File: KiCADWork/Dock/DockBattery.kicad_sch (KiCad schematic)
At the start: 0 parts

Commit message: Dock Updates
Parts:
- added BT2: Battery, easyeda2kicad:CONN-TH_S2B-PH-K-LF-SN, symbol Device:Battery
- added C1, C3: 10u, Capacitor_SMD:C_0402_1005Metric_Pad0.74x0.62mm_HandSolder, symbol Device:C
- added C2 (x2): 1u, Capacitor_SMD:C_0402_1005Metric_Pad0.74x0.62mm_HandSolder, symbol Device:C
- added C2: 100n, Capacitor_SMD:C_0402_1005Metric_Pad0.74x0.62mm_HandSolder, symbol Device:C
- added D1: WHITE LED, LED_SMD:LED_0603_1608Metric_Pad1.05x0.95mm_HandSolder, symbol Device:LED
- added R1, R3: 2k, Resistor_SMD:R_0402_1005Metric_Pad0.72x0.64mm_HandSolder, symbol Device:R
- added R2: 100, Resistor_SMD:R_0402_1005Metric_Pad0.72x0.64mm_HandSolder, symbol Device:R
- added U1: MCP73831T-2ACI/OT, easyeda2kicad:SOT-23-5_L3.0-W1.7-P0.95-LS2.8-BL, symbol easyeda2kicad:MCP73831T-2ACI_OT
- added U2: XB6096I2SV, easyeda2kicad:WDFN-6_L2.0-W2.0-P0.65-BL-EP, symbol easyeda2kicad:XB6096I2SV
- added U4: PJ9193M33SE, easyeda2kicad:SSOP-5_L2.9-W1.6-P0.95-LS2.8-BR, symbol easyeda2kicad:PJ9193M33SE
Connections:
- new net: R3.1, U1.5 (PROG)
- new net: D1.1 (K), R1.1
- new net: R1.2, U1.1 (STAT)
- new net: BT2.1 (+), R2.1
- new net: BT2.2 (-), U2.2 (GND), U2.3 (GND), U2.7 (EP)
- new net +3V3: C2.1, U4.5 (VOUT)
- new net GND: C1.2, C2.2, C2.2, C2.2, C3.2, R3.2, U1.2 (VSS), U2.4 (VM), U2.5 (VM), U2.6 (VM), U4.2 (GND)
- new net VBAT: C1.1, C2.1, C2.1, R2.2, U1.3 (VBAT), U2.1 (VDD), U4.1 (VIN), U4.3 (EN)
- new net VBUS: C3.1, D1.2 (A), U1.4 (VDD)
- no-connect marks 0 -> 1

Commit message: Ignoring Backups
More Dock progress
All local backups removed
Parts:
- removed C1, C3: 10u, Capacitor_SMD:C_0402_1005Metric_Pad0.74x0.62mm_HandSolder, symbol Device:C
- removed C2: 100n, Capacitor_SMD:C_0402_1005Metric_Pad0.74x0.62mm_HandSolder, symbol Device:C
- removed D1: WHITE LED, LED_SMD:LED_0603_1608Metric_Pad1.05x0.95mm_HandSolder, symbol Device:LED
- removed R1, R3: 2k, Resistor_SMD:R_0402_1005Metric_Pad0.72x0.64mm_HandSolder, symbol Device:R
- removed R2: 100, Resistor_SMD:R_0402_1005Metric_Pad0.72x0.64mm_HandSolder, symbol Device:R
- removed U1: MCP73831T-2ACI/OT, easyeda2kicad:SOT-23-5_L3.0-W1.7-P0.95-LS2.8-BL, symbol easyeda2kicad:MCP73831T-2ACI_OT
- removed U2: XB6096I2SV, easyeda2kicad:WDFN-6_L2.0-W2.0-P0.65-BL-EP, symbol easyeda2kicad:XB6096I2SV
- removed U4: PJ9193M33SE, easyeda2kicad:SSOP-5_L2.9-W1.6-P0.95-LS2.8-BR, symbol easyeda2kicad:PJ9193M33SE
- added C12, C6: 4.7u, Capacitor_SMD:C_0402_1005Metric_Pad0.74x0.62mm_HandSolder, symbol Device:C
- added C15: 10u, Capacitor_SMD:C_0402_1005Metric_Pad0.74x0.62mm_HandSolder, symbol Device:C
- added C16, C17: 22u, Capacitor_SMD:C_0603_1608Metric_Pad1.08x0.95mm_HandSolder, symbol Device:C
- added C5: 1u, Capacitor_SMD:C_0402_1005Metric_Pad0.74x0.62mm_HandSolder, symbol Device:C
- added D1: BLUE RED, LED_SMD:LED_0603_1608Metric_Pad1.05x0.95mm_HandSolder, symbol Device:LED
- added D1: BLUE LED, LED_SMD:LED_0603_1608Metric_Pad1.05x0.95mm_HandSolder, symbol Device:LED
- added L1: 4.7u, easyeda2kicad:IND-SMD_L5.2-W5.2_YSPI0530, symbol Device:L
- added R12: 100k, Resistor_SMD:R_0402_1005Metric_Pad0.72x0.64mm_HandSolder, symbol Device:R
- added R12: 1.78k, Resistor_SMD:R_0402_1005Metric_Pad0.72x0.64mm_HandSolder, symbol Device:R
- added R12 (x3): 1.18k, Resistor_SMD:R_0402_1005Metric_Pad0.72x0.64mm_HandSolder, symbol Device:R
- added R12: 10k, Resistor_SMD:R_0402_1005Metric_Pad0.72x0.64mm_HandSolder, symbol Device:R
- added R12: 732, Resistor_SMD:R_0402_1005Metric_Pad0.72x0.64mm_HandSolder, symbol Device:R
- added U2: TPS61023DRLR, easyeda2kicad:SOT-563_L1.6-W1.2-P0.50-LS1.6-BR, symbol easyeda2kicad:TPS61023DRLR
- added U3: AMS1117-3.3, Package_TO_SOT_SMD:SOT-223-3_TabPin2, symbol Regulator_Linear:AMS1117-3.3
- added U4: BQ24073RGT, Package_DFN_QFN:VQFN-16-1EP_3x3mm_P0.5mm_EP1.6x1.6mm, symbol Battery_Management:BQ24073RGT
- BT2: LCSC Part (none) -> C173752
- C13, C14: renamed from C2; value 1u -> 2.2u; LCSC Part (none) -> C12530
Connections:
- net +3V3: now also U3.2 (VO)
- net GND: now also BT2.2 (-), C12.2, C15.2, C16.2, C17.2, C5.2, C6.2, R12.1, R12.1, R12.2, R12.2, U2.4 (GND), U3.1 (GND), U4.14 (TMR), U4.17 (VSS), U4.4 (~{CE}), U4.6 (EN1), U4.8 (VSS)
- net VBUS: now also C5.1, U4.13 (IN)
- net at BT2.1 (+): now also C12.1, U4.2 (BAT), U4.3 (BAT)
- net VBAT renamed Vsys
- net Vsys: now also C16.1, C17.1, R12.2, R12.2, U2.6 (VOUT), U3.3 (VI)
- new net: L1.1, U2.3 (VIN)
- new net: C15.1, C6.1, L1.2, R12.2, R12.2, U2.2 (EN), U2.5 (SW), U4.10 (OUT), U4.11 (OUT), U4.5 (EN2)
- new net: R12.1, U4.16 (ISET)
- new net: D1.2 (A), R12.1 (x2)
- new net: D1.1 (K), U4.7 (~{PGOOD})
- new net: R12.1, U2.1 (FB)
- new net: D1.1 (K), U4.9 (~{CHG})
- new net: R12.2, U4.1 (TS)
- new net: R12.1, U4.12 (ILIM)
- no-connect marks 1 -> 0
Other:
- moved on the sheet: BT2, C13, C14

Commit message: Beautiful Skilkscreen Added
Dock schematic intial draft complete
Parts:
- added D5: LED, LED_SMD:LED_0603_1608Metric_Pad1.05x0.95mm_HandSolder, symbol Device:LED
- added R12: 2k, Resistor_SMD:R_0402_1005Metric_Pad0.72x0.64mm_HandSolder, symbol Device:R
- added TP1 (x5): TestPoint, TestPoint:TestPoint_Pad_D1.0mm, symbol Connector:TestPoint
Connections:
- net +3V3: now also R12.2, TP1.1
- net GND: now also D5.1 (K)
- net VBUS: now also TP1.1
- net Vsys: now also TP1.1
- net at C15.1, C6.1, L1.2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: now also TP1.1
- net at BT2.1 (+), C12.1, U4.2 (BAT)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: now also TP1.1
- new net: D5.2 (A), R12.1

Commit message: Small Updates
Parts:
- D1: footprint LED_SMD:LED_0603_1608Metric_Pad1.05x0.95mm_HandSolder -> easyeda2kicad:SideStuckLED
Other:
- moved on the sheet: D5, R12
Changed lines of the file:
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@@
     (stroke (width 0) (type default))
   )
-  (wire (pts (xy 117.475 153.035) (xy 117.475 160.655))
+  (wire (pts (xy 108.585 163.83) (xy 108.585 171.45))
     (stroke (width 0) (type default))
   )
@@
     (stroke (width 0) (type default))
   )
-  (wire (pts (xy 117.475 139.7) (xy 117.475 145.415))
+  (wire (pts (xy 108.585 150.495) (xy 108.585 156.21))
     (stroke (width 0) (type default))
   )
@@
     (stroke (width 0) (type default))
   )
-  (wire (pts (xy 117.475 130.81) (xy 117.475 132.08))
+  (wire (pts (xy 108.585 141.605) (xy 108.585 142.875))
     (stroke (width 0) (type default))
   )
@@
     (effects (font (size 3 3)) (justify left bottom))
   )
-  (label "Power Indicator" (at 120.015 146.05 0) (fields_autoplaced)
+  (label "Power Indicator" (at 111.125 156.845 0) (fields_autoplaced)
     (effects (font (size 2 2)) (justify left bottom))
   )
@@
     (effects (font (size 1.27 1.27)) (justify right))
   )
-  (symbol (lib_id "Device:LED") (at 117.475 149.225 90) (unit 1)
-    (in_bom yes) (on_board yes) (dnp no) (fields_autoplaced)
-    (property "Reference" "D5" (at 120.65 149.5425 90)
+  (symbol (lib_id "Device:LED") (at 108.585 160.02 90) (unit 1)
+    (in_bom yes) (on_board yes) (dnp no) (fields_autoplaced)
+    (property "Reference" "D5" (at 111.76 160.3375 90)
       (effects (font (size 1.27 1.27)) (justify right))
     )
-    (property "Value" "LED" (at 120.65 152.0825 90)
+    (property "Value" "LED" (at 111.76 162.8775 90)
       (effects (font (size 1.27 1.27)) (justify right))
     )
-    (property "Footprint" "LED_SMD:LED_0603_1608Metric_Pad1.05x0.95mm_HandSolder" (at 117.475 149.225 0)
-      (effects (font (size 1.27 1.27)) hide)
-    )
-    (property "Datasheet" "~" (at 117.475 149.225 0)
+    (property "Footprint" "LED_SMD:LED_0603_1608Metric_Pad1.05x0.95mm_HandSolder" (at 108.585 160.02 0)
+      (effects (font (size 1.27 1.27)) hide)
+    )
+    (property "Datasheet" "~" (at 108.585 160.02 0)
       (effects (font (size 1.27 1.27)) hide)
     )
@@
     )
   )
-  (symbol (lib_id "power:GND") (at 117.475 160.655 0) (unit 1)
-    (in_bom yes) (on_board yes) (dnp no) (fields_autoplaced)
-    (property "Reference" "#PWR023" (at 117.475 167.005 0)
-      (effects (font (size 1.27 1.27)) hide)
-    )
-    (property "Value" "GND" (at 117.475 165.735 0)
-      (effects (font (size 1.27 1.27)))
-    )
-    (property "Footprint" "" (at 117.475 160.655 0)
-      (effects (font (size 1.27 1.27)) hide)
-    )
-    (property "Datasheet" "" (at 117.475 160.655 0)
+  (symbol (lib_id "power:GND") (at 108.585 171.45 0) (unit 1)
+    (in_bom yes) (on_board yes) (dnp no) (fields_autoplaced)
+    (property "Reference" "#PWR023" (at 108.585 177.8 0)
+      (effects (font (size 1.27 1.27)) hide)
+    )
+    (property "Value" "GND" (at 108.585 176.53 0)
+      (effects (font (size 1.27 1.27)))
+    )
+    (property "Footprint" "" (at 108.585 171.45 0)
+      (effects (font (size 1.27 1.27)) hide)
+    )
+    (property "Datasheet" "" (at 108.585 171.45 0)
       (effects (font (size 1.27 1.27)) hide)
     )
@@
       (effects (font (size 1.27 1.27)) (justify left))
     )
-    (property "Footprint" "LED_SMD:LED_0603_1608Metric_Pad1.05x0.95mm_HandSolder" (at 127 77.47 0)
+    (property "Footprint" "easyeda2kicad:SideStuckLED" (at 127 77.47 0)
       (effects (font (size 1.27 1.27)) hide)
     )
@@
       (effects (font (size 1.27 1.27)) (justify left))
     )
-    (property "Footprint" "LED_SMD:LED_0603_1608Metric_Pad1.05x0.95mm_HandSolder" (at 137.16 78.105 0)
+    (property "Footprint" "easyeda2kicad:SideStuckLED" (at 137.16 78.105 0)
       (effects (font (size 1.27 1.27)) hide)
     )
@@
     )
   )
-  (symbol (lib_id "Device:R") (at 117.475 135.89 180) (unit 1)
-    (in_bom yes) (on_board yes) (dnp no)
-    (property "Reference" "R12" (at 112.395 135.89 90)
-      (effects (font (size 1.27 1.27)))
-    )
-    (property "Value" "2k" (at 114.935 135.89 90)
-      (effects (font (size 1.27 1.27)))
-    )
-    (property "Footprint" "Resistor_SMD:R_0402_1005Metric_Pad0.72x0.64mm_HandSolder" (at 119.253 135.89 90)
-      (effects (font (size 1.27 1.27)) hide)
-    )
-    (property "Datasheet" "~" (at 117.475 135.89 0)
-      (effects (font (size 1.27 1.27)) hide)
-    )
-    (property "LCSC Part" "C3016052" (at 117.475 135.89 0)
+  (symbol (lib_id "Device:R") (at 108.585 146.685 180) (unit 1)
+    (in_bom yes) (on_board yes) (dnp no)
+    (property "Reference" "R12" (at 103.505 146.685 90)
+      (effects (font (size 1.27 1.27)))
+    )
+    (property "Value" "2k" (at 106.045 146.685 90)
+      (effects (font (size 1.27 1.27)))
+    )
+    (property "Footprint" "Resistor_SMD:R_0402_1005Metric_Pad0.72x0.64mm_HandSolder" (at 110.363 146.685 90)
+      (effects (font (size 1.27 1.27)) hide)
+    )
+    (property "Datasheet" "~" (at 108.585 146.685 0)
+      (effects (font (size 1.27 1.27)) hide)
+    )
+    (property "LCSC Part" "C3016052" (at 108.585 146.685 0)
       (effects (font (size 1.27 1.27)) hide)
     )
@@
     )
   )
-  (symbol (lib_id "power:+3V3") (at 117.475 130.81 0) (unit 1)
-    (in_bom yes) (on_board yes) (dnp no) (fields_autoplaced)
-    (property "Reference" "#PWR022" (at 117.475 134.62 0)
-      (effects (font (size 1.27 1.27)) hide)
-    )
-    (property "Value" "+3V3" (at 117.475 125.73 0)
-      (effects (font (size 1.27 1.27)))
-    )
-    (property "Footprint" "" (at 117.475 130.81 0)
-      (effects (font (size 1.27 1.27)) hide)
-    )
-    (property "Datasheet" "" (at 117.475 130.81 0)
-      (effects (font (size 1.27 1.27)) hide)
-    )
+  (symbol (lib_id "power:+3V3") (at 108.585 141.605 0) (unit 1)
+    (in_bom yes) (on_board yes) (dnp no) (fields_autoplaced)
+    (property "Reference" "#PWR022" (at 108.585 145.415 0)
+      (effects (font (size 1.27 1.27)) hide)
+    )
+    (property "Value" "+3V3" (at 108.585 136.525 0)
+      (effects (font (size 1.27 1.27)))
+    )
+    (property "Footprint" "" (at 108.585 141.605 0)
+      (effects (font (size 1.27 1.27)) hide)
+    )
+    (property "Datasheet" "" (at 108.585 141.605 0)
+      (effects (font (size 1.27 1.27)) hide)
+    )

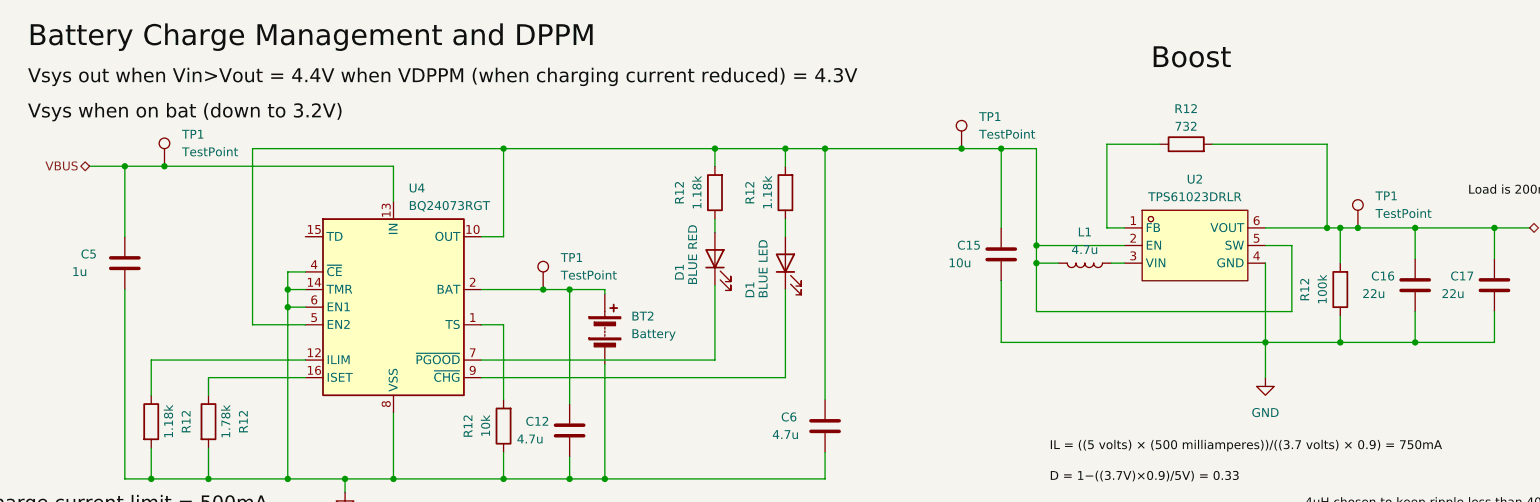
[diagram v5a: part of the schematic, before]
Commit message: Dock Updates
Starting to layout the dock
Dom still to check
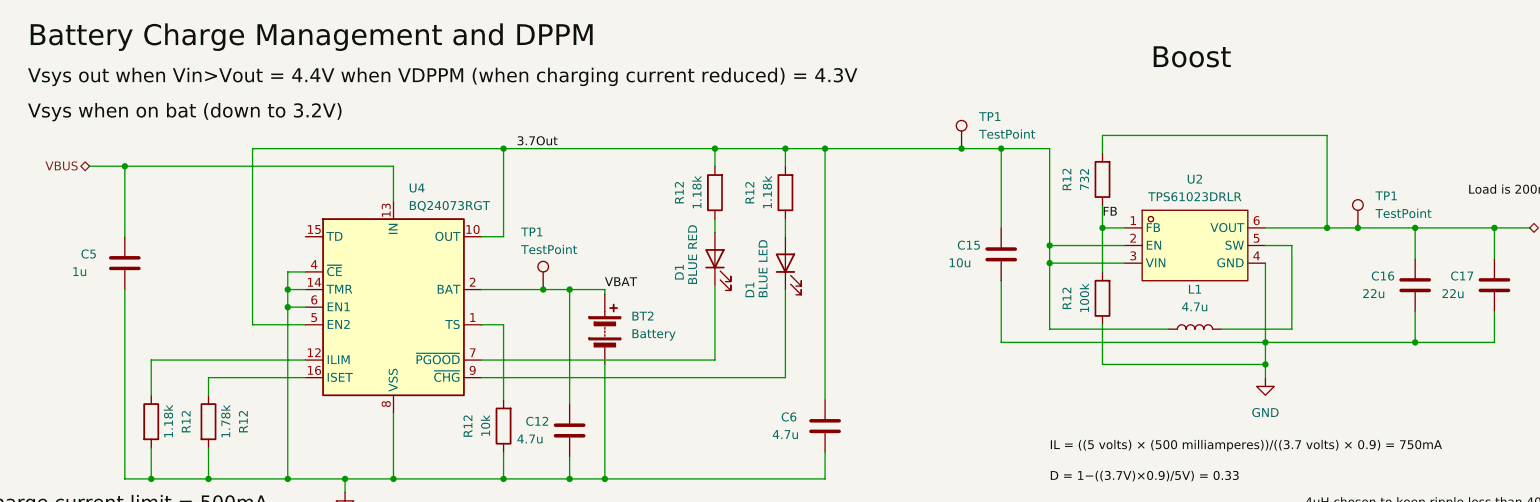
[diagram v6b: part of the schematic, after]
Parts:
- removed TP1: TestPoint, TestPoint:TestPoint_Pad_D1.0mm, symbol Connector:TestPoint
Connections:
- net Vsys: no longer R12.2
- net 3.7Out: now reaches L1.1, U2.3 (VIN)
- net 3.7Out: now also C15.1, C6.1, R12.2, R12.2, TP1.1, U2.2 (EN), U4.10 (OUT), U4.11 (OUT), U4.5 (EN2)
- net VBAT: now reaches BT2.1 (+), C12.1, TP1.1, U4.2 (BAT), U4.3 (BAT)
- net FB: now reaches R12.1, U2.1 (FB)
- net FB: now also R12.2
- new net: L1.2, U2.5 (SW)
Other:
- moved on the sheet: L1, R12

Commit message: Initial Dock DRC Complete
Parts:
- BT2: footprint easyeda2kicad:CONN-TH_S2B-PH-K-LF-SN -> easyeda2kicad:CONN-TH_S2B-PH-K-S-LF-SN
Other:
- moved on the sheet: D1
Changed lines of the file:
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@@
     (stroke (width 0) (type default))
   )
-  (wire (pts (xy 244.475 73.025) (xy 239.395 73.025))
+  (wire (pts (xy 257.175 73.025) (xy 239.395 73.025))
     (stroke (width 0) (type default))
   )
@@
     (stroke (width 0) (type default))
   )
-  (wire (pts (xy 137.16 74.295) (xy 137.16 71.755))
+  (wire (pts (xy 137.16 73.66) (xy 137.16 71.755))
     (stroke (width 0) (type default))
   )
@@
     (stroke (width 0) (type default))
   )
-  (wire (pts (xy 137.16 81.915) (xy 137.16 94.615))
+  (wire (pts (xy 137.16 81.28) (xy 137.16 94.615))
     (stroke (width 0) (type default))
   )
@@
     (effects (font (size 1.27 1.27)) (justify right))
   )
-  (hierarchical_label "Vsys" (shape bidirectional) (at 244.475 73.025 0) (fields_autoplaced)
+  (hierarchical_label "Vsys" (shape bidirectional) (at 257.175 73.025 0) (fields_autoplaced)
     (effects (font (size 1.27 1.27)) (justify left))
   )
@@
       (effects (font (size 1.27 1.27)) (justify left))
     )
-    (property "Footprint" "easyeda2kicad:CONN-TH_S2B-PH-K-LF-SN" (at 111.125 86.106 90)
+    (property "Footprint" "easyeda2kicad:CONN-TH_S2B-PH-K-S-LF-SN" (at 111.125 86.106 90)
       (effects (font (size 1.27 1.27)) hide)
     )
@@
     )
   )
-  (symbol (lib_id "Device:LED") (at 137.16 78.105 90) (unit 1)
-    (in_bom yes) (on_board yes) (dnp no)
-    (property "Reference" "D1" (at 132.08 83.185 0)
-      (effects (font (size 1.27 1.27)) (justify left))
-    )
-    (property "Value" "BLUE LED" (at 133.985 83.185 0)
-      (effects (font (size 1.27 1.27)) (justify left))
-    )
-    (property "Footprint" "easyeda2kicad:SideStuckLED" (at 137.16 78.105 0)
-      (effects (font (size 1.27 1.27)) hide)
-    )
-    (property "Datasheet" "~" (at 137.16 78.105 0)
-      (effects (font (size 1.27 1.27)) hide)
-    )
-    (property "LCSC Part" "C7371904 " (at 137.16 78.105 0)
-      (effects (font (size 1.27 1.27)) hide)
-    )
+  (symbol (lib_id "Device:LED") (at 137.16 77.47 90) (unit 1)
+    (in_bom yes) (on_board yes) (dnp no)
+    (property "Reference" "D1" (at 132.08 82.55 0)
+      (effects (font (size 1.27 1.27)) (justify left))
+    )
+    (property "Value" "BLUE LED" (at 133.985 82.55 0)
+      (effects (font (size 1.27 1.27)) (justify left))
+    )
+    (property "Footprint" "easyeda2kicad:SideStuckLED" (at 137.16 77.47 0)
+      (effects (font (size 1.27 1.27)) hide)
+    )
+    (property "Datasheet" "~" (at 137.16 77.47 0)
+      (effects (font (size 1.27 1.27)) hide)
+    )
+    (property "LCSC Part" "C7371904 " (at 137.16 77.47 0)
+      (effects (font (size 1.27 1.27)) hide)
+    )
